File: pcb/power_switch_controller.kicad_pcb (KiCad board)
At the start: 2 copper layers, 116.8 x 53.3 mm, 19 parts, among them J1 DB15FV, J2 DB15FV, P1 PWR_JACK_2.5x5.5, P2 HEADER_01X03, U1 MAX6817

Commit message: Made design changes preparing for version 1.0.
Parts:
- removed J1, J2: DB15FV, aalborg_mfc_interface:DB15FD
- removed R3, R4: 5.11k, aalborg_mfc_interface:SM1210
- added D10, D6, D7, D8, D9: LED_24V, power_switch_controller:LED_555-3XXX, F.Cu at (152.4, 139.7)
- added D11: LED_24V, power_switch_controller:LED_555-3XXX, F.Cu at (130.8, 153.7)
- added D12: LED_24V, power_switch_controller:LED_555-3XXX, F.Cu at (123.2, 154.3)
- added D13: LED_24V, power_switch_controller:LED_555-3XXX, F.Cu at (114.9, 155.6)
- added D14: LED_24V, power_switch_controller:LED_555-3XXX, F.Cu at (104.8, 144.8)
- added D15: LED_24V, power_switch_controller:LED_555-3XXX, F.Cu at (165.7, 137.2)
- added D16: LED_24V, power_switch_controller:LED_555-3XXX, F.Cu at (122.6, 142.2)
- added D17: LED_24V, power_switch_controller:LED_555-3XXX, F.Cu at (139.1, 140.3)
- added D2: LED_24V, power_switch_controller:LED_555-3XXX, F.Cu at (181.0, 99.7)
- added D3: LED_24V, power_switch_controller:LED_555-3XXX, F.Cu at (172.1, 99.7)
- added D4: LED_24V, power_switch_controller:LED_555-3XXX, F.Cu at (163.2, 99.7)
- added D5: LED_24V, power_switch_controller:LED_555-3XXX, F.Cu at (154.3, 99.7)
- added RJ1: RJ45_DOUBLE, power_switch_controller:RJ45_2PORT_2ROW, F.Cu at (97.2, 94.0)
- added RJ2: RJ45_DOUBLE, power_switch_controller:RJ45_2PORT_2ROW, F.Cu at (97.2, 111.8)
- added S1: HEADER_01X02_POL, power_switch_controller:Header_Shrouded_2_Pin, F.Cu at (181.0, 95.9)
- added S10: HEADER_01X02_POL, power_switch_controller:Header_Shrouded_2_Pin, F.Cu at (153.0, 155.6)
- added S11: HEADER_01X02_POL, power_switch_controller:Header_Shrouded_2_Pin, F.Cu at (151.1, 163.8)
- added S12: HEADER_01X02_POL, power_switch_controller:Header_Shrouded_2_Pin, F.Cu at (144.1, 152.4)
- added S13: HEADER_01X02_POL, power_switch_controller:Header_Shrouded_2_Pin, F.Cu at (178.4, 142.2)
- added S14, S15, S16: HEADER_01X02_POL, power_switch_controller:Header_Shrouded_2_Pin, F.Cu at (179.7, 150.4)
- added S2: HEADER_01X02_POL, power_switch_controller:Header_Shrouded_2_Pin, F.Cu at (172.1, 95.9)
- added S3: HEADER_01X02_POL, power_switch_controller:Header_Shrouded_2_Pin, F.Cu at (163.2, 95.9)
- added S4: HEADER_01X02_POL, power_switch_controller:Header_Shrouded_2_Pin, F.Cu at (154.3, 95.9)
- added S5: HEADER_01X02_POL, power_switch_controller:Header_Shrouded_2_Pin, F.Cu at (145.4, 95.9)
- added S6: HEADER_01X02_POL, power_switch_controller:Header_Shrouded_2_Pin, F.Cu at (136.5, 95.9)
- added S7: HEADER_01X02_POL, power_switch_controller:Header_Shrouded_2_Pin, F.Cu at (177.2, 158.8)
- added S8: HEADER_01X02_POL, power_switch_controller:Header_Shrouded_2_Pin, F.Cu at (167.0, 151.8)
- added S9: HEADER_01X02_POL, power_switch_controller:Header_Shrouded_2_Pin, F.Cu at (164.5, 161.9)
- added SW1: SPST_SERIES_M, power_switch_controller:SPST_SERIES_M, F.Cu at (202.6, 83.2)
- added U2: TLE723X, power_switch_controller:TLE723X, B.Cu at (149.9, 87.0)
- added U3: TLE723X, power_switch_controller:TLE723X, B.Cu at (149.9, 109.2)
- ARDUINO1: footprint aalborg_mfc_interface:ARDUINO_MEGA_SHIELD -> power_switch_controller:ARDUINO_MEGA_SHIELD
- C1, C2, C3, C4, R1, R2: footprint aalborg_mfc_interface:SM1210 -> power_switch_controller:SM1210
- C5: value 10uF -> 0.1uF; footprint aalborg_mfc_interface:SM1210 -> power_switch_controller:SM1210; moved to F.Cu
- C6: value 10uF -> 0.1uF; footprint aalborg_mfc_interface:SM1210 -> power_switch_controller:SM1210
- D1: footprint aalborg_mfc_interface:LED_555-3XXX -> power_switch_controller:LED_555-3XXX
- E1: footprint aalborg_mfc_interface:Micro-MaTch_6_SMD -> power_switch_controller:Micro-MaTch_6_SMD
- P1: footprint aalborg_mfc_interface:DCJACK_2PIN_HIGHCURRENT -> power_switch_controller:DCJACK_2PIN_HIGHCURRENT
- P2: footprint aalborg_mfc_interface:Header_Shrouded_3_Pin -> power_switch_controller:Header_Shrouded_3_Pin
- REG1: footprint aalborg_mfc_interface:DC_DC_CONV_R78C -> power_switch_controller:DC_DC_CONV_R78C
- U1: footprint aalborg_mfc_interface:MAX6817 -> power_switch_controller:MAX6817
- moved C5 77.7 mm to (202.6, 140.3), turned to 270 degrees
- moved D1 2.29 mm to (202.6, 92.7)
- moved C3 2.01 mm to (104.8, 127.0), turned to 180 degrees
- moved P2 2.01 mm to (103.5, 123.2)
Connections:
- ARDUINO1 pad 22: /PURGE_A -> (no net)
- ARDUINO1 pad 23: /VALVE_OFF_A -> (no net)
- ARDUINO1 pad 24: /PURGE_B -> (no net)
- ARDUINO1 pad 25: /VALVE_OFF_B -> (no net)
- ARDUINO1 pad 48: (no net) -> /IN
- ARDUINO1 pad 49: (no net) -> /CS
- ARDUINO1 pad 50: (no net) -> /MISO
- ARDUINO1 pad 51: (no net) -> /MOSI
- ARDUINO1 pad 52: (no net) -> /SCK
- ARDUINO1 pad 7: /PWM_A -> (no net)
- ARDUINO1 pad 8: /PWM_B -> (no net)
- ARDUINO1 pad A0: /ANALOG_IN_A -> (no net)
- ARDUINO1 pad A1: /ANALOG_IN_B -> (no net)
- ARDUINO1 pad RST: (no net) -> /RST
- C5 pad 1: /ANALOG_OUT_A -> +5V
- C6 pad 1: /ANALOG_OUT_B -> +5V
- D1 pad 1: VAA -> /LED_PWR
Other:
- board text added: "Janelia Remote Device power_switch_controller model_number: 1101 01/2015 version 1.0"
- board text removed: "Janelia Remote Device aalborg_mfc_interface model_number: 1100 12/2014 version 1.1"
- board text removed: "MFCA"
- board text removed: "MFCB"

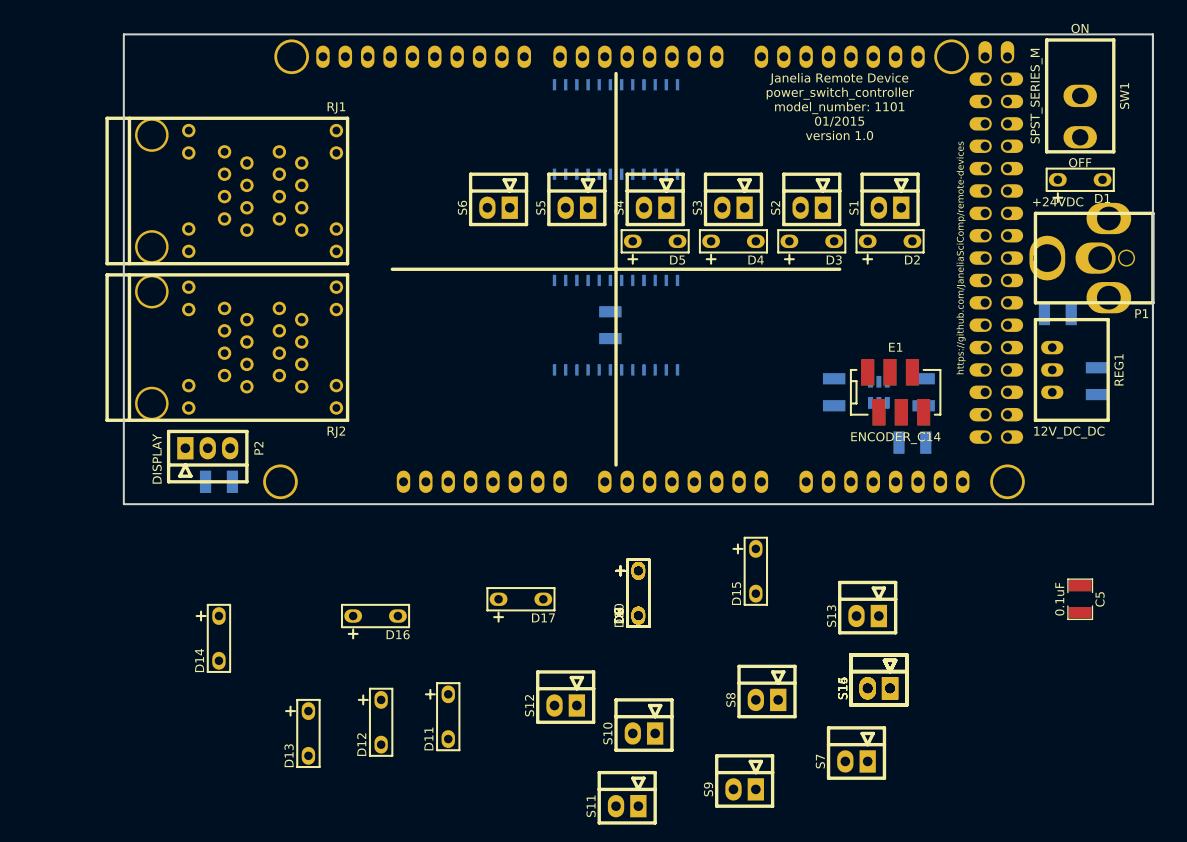
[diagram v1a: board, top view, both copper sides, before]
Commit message: Changed connectors to 2x16 header.
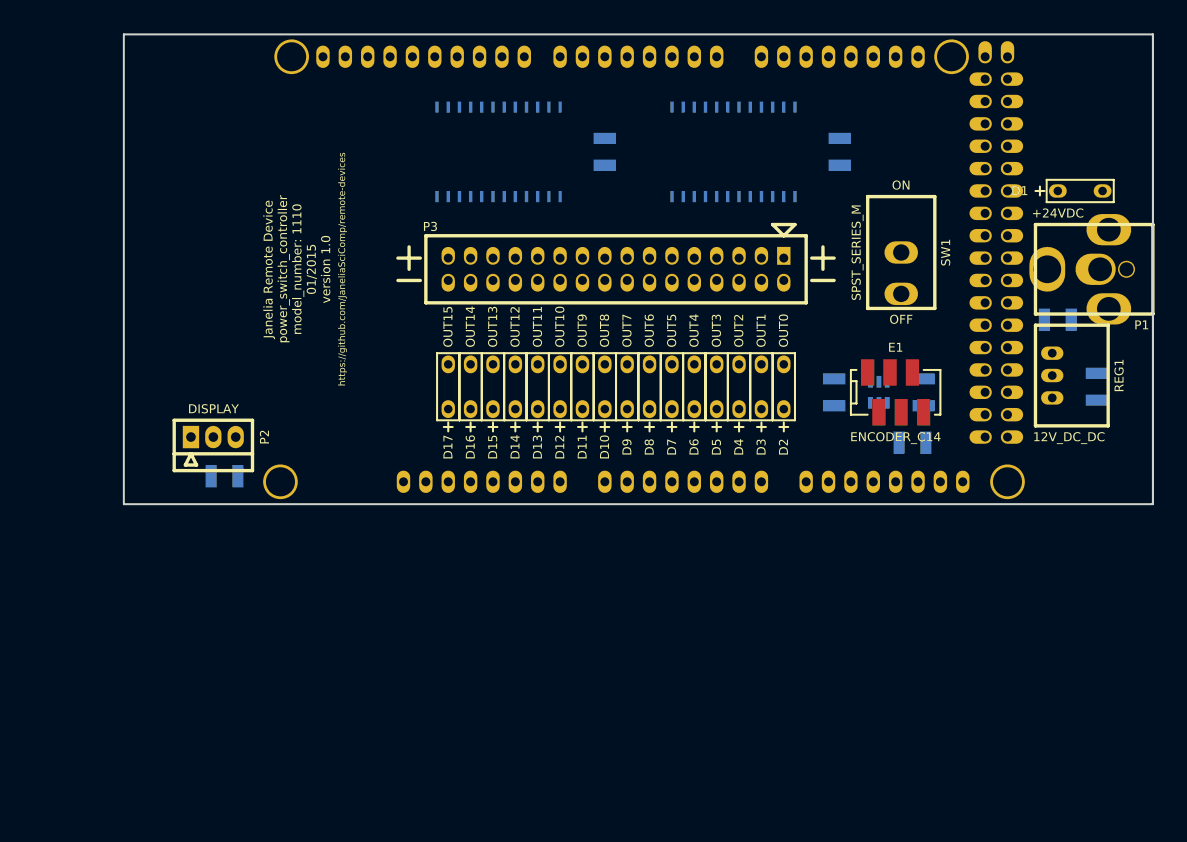
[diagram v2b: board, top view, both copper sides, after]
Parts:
- removed RJ1, RJ2: RJ45_DOUBLE, power_switch_controller:RJ45_2PORT_2ROW
- removed S1, S10, S11, S12, S13, S14, S15, S16, S2, S3, S4, S5, S6, S7, S8, S9: HEADER_01X02_POL, power_switch_controller:Header_Shrouded_2_Pin
- added P3: HEADER_02X16, power_switch_controller:HEADER_02x32, F.Cu at (149.9, 102.9)
- C5: moved to B.Cu
- moved C5 57.7 mm to (175.3, 89.5)
- moved D13 47.2 mm to (141.0, 116.2), turned to 180 degrees
- moved D14 44.1 mm to (138.4, 116.2), turned to 180 degrees
- moved D12 43.2 mm to (143.5, 116.2), turned to 180 degrees
- moved D11 40.4 mm to (146.1, 116.2), turned to 180 degrees
- moved D15 36.5 mm to (135.9, 116.2), turned to 180 degrees
- moved D16 28.2 mm to (133.3, 116.2), turned to 180 degrees
- moved SW1 27.0 mm to (182.2, 101.0)
- moved D17 25.5 mm to (130.8, 116.2), turned to 180 degrees
- moved D6 24.3 mm to (158.8, 116.2), turned to 180 degrees
- moved U3 23.8 mm to (136.5, 89.5)
- moved D10 23.8 mm to (148.6, 116.2), turned to 180 degrees
- moved D7 23.8 mm to (156.2, 116.2), turned to 180 degrees
- moved D8 23.5 mm to (153.7, 116.2), turned to 180 degrees
- moved D9 23.5 mm to (151.1, 116.2), turned to 180 degrees
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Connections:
- net /SO1 renamed /SI1
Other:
- board text added: "Janelia Remote Device power_switch_controller model_number: 1110 01/2015 version 1.0"
- board text added: "OUT0"
- board text added: "OUT1"
- board text added: "OUT10"
- board text added: "OUT11"
- board text added: "OUT12"
- board text added: "OUT13"
- board text added: "OUT14"
- board text added: "OUT15"
- board text added: "OUT2"
- board text added: "OUT3"
- board text added: "OUT4"
- board text added: "OUT5"
- board text added: "OUT6"
- board text added: "OUT7"
- board text added: "OUT8"
- board text added: "OUT9"
- board text removed: "Janelia Remote Device power_switch_controller model_number: 1101 01/2015 version 1.0"

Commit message: Moved components on pcb.
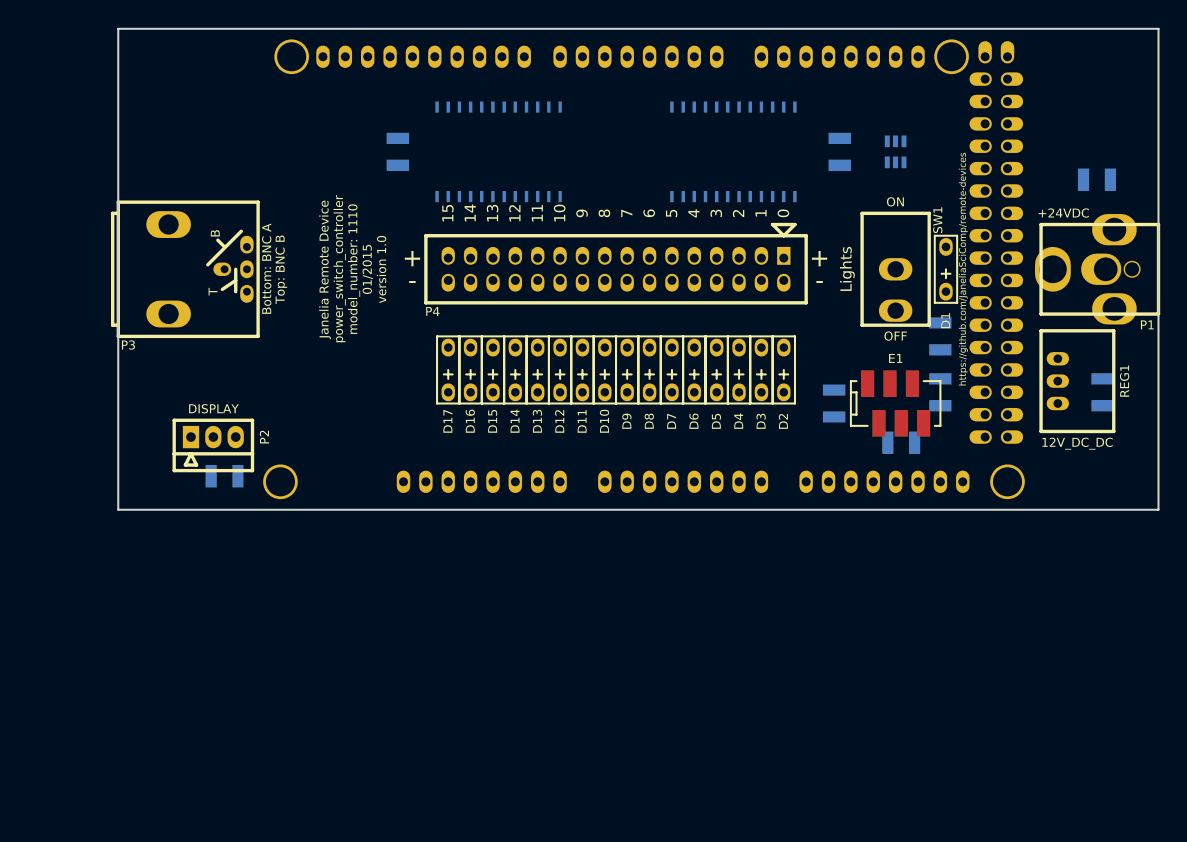
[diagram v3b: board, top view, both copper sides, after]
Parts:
- added P4: HEADER_02X16, power_switch_controller:HEADER_02x32, F.Cu at (149.9, 102.9)
- added R3: 5.11k, power_switch_controller:SM1210, B.Cu at (186.7, 110.5)
- P3: value HEADER_02X16 -> BNC_DOUBLE_RA; footprint power_switch_controller:HEADER_02x32 -> power_switch_controller:BNC_DOUBLE
- moved P3 50.8 mm to (99.1, 102.9), turned to 90 degrees
- moved U1 27.4 mm to (181.6, 89.5), turned to 90 degrees
- moved C6 23.5 mm to (125.1, 89.5), turned to 90 degrees
- moved D1 17.6 mm to (187.3, 102.9), turned to 180 degrees
- moved C1 16.5 mm to (204.5, 92.7)
- moved R2 9.94 mm to (174.6, 118.1), turned to 270 degrees
- moved C4 9.53 mm to (182.2, 122.6), turned to 180 degrees
- moved SW1 2.01 mm to (181.6, 102.9)
- moved D10 1.91 mm to (148.6, 114.3)
- moved D11 1.91 mm to (146.1, 114.3)
- moved D12 1.91 mm to (143.5, 114.3)
- moved D13 1.91 mm to (141.0, 114.3)
- moved D14 1.91 mm to (138.4, 114.3)
- moved D15 1.91 mm to (135.9, 114.3)
- moved D16 1.91 mm to (133.3, 114.3)
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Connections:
- ARDUINO1 pad 18: (no net) -> /D_LED_PWR
- ARDUINO1 pad 20: Net-(ARDUINO1-Pad20) -> (no net)
- ARDUINO1 pad 21: Net-(ARDUINO1-Pad21) -> (no net)
- P3 pad 1: VAA -> /BNC_A
- P3 pad 2: /OUT0 -> GND
- P3 pad 3: VAA -> /BNC_B
- P3 pad 4: /OUT1 -> GND
- U1 pad 3: (no net) -> /LED_PWR
- U1 pad 4: (no net) -> /D_LED_PWR
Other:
- board size 116.8 x 53.3 mm -> 118.1 x 54.6 mm
- net class SUPERPOWER added: clearance 0.254, trace_width 1.2192, via_dia 0.889, via_drill 0.635
- board text removed: "OUT0"
- board text removed: "OUT1"
- board text removed: "OUT10"
- board text removed: "OUT11"
- board text removed: "OUT12"
- board text removed: "OUT13"
- board text removed: "OUT14"
- board text removed: "OUT15"
- board text removed: "OUT2"
- board text removed: "OUT3"
- board text removed: "OUT4"
- board text removed: "OUT5"
- board text removed: "OUT6"
- board text removed: "OUT7"
- board text removed: "OUT8"
- board text removed: "OUT9"

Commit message: Finished pcb version 1.0
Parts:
- added P5: HEADER_02X08, power_switch_controller:HEADER_02x08, F.Cu at (129.5, 102.9)
- P4: value HEADER_02X16 -> HEADER_02X08; footprint power_switch_controller:HEADER_02x32 -> power_switch_controller:HEADER_02x08
- moved D11 10.2 mm to (135.9, 114.9)
- moved D10 10.2 mm to (138.4, 114.9)
- moved D12 10.2 mm to (133.3, 114.9)
- moved D13 10.2 mm to (130.8, 114.9)
- moved D14 10.2 mm to (128.3, 114.9)
- moved D16 10.2 mm to (123.2, 114.9)
- moved D17 10.2 mm to (120.7, 114.9)
- moved D15 10.2 mm to (125.7, 114.9)
- moved P4 10.2 mm to (160.0, 102.9)
- moved C6 7.62 mm to (117.5, 89.5)
- moved U3 6.99 mm to (129.5, 89.5)
- moved C5 3.17 mm to (172.1, 89.5)
- moved U2 3.17 mm to (160.0, 89.5)
- moved D2 0.64 mm to (168.9, 114.9)
- moved D3 0.64 mm to (166.4, 114.9)
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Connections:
- ARDUINO1 pad 10: (no net) -> /BNC_B
- ARDUINO1 pad 20B: /BNC_B -> (no net)
- ARDUINO1 pad 21B: /BNC_A -> (no net)
- ARDUINO1 pad A0: (no net) -> /BNC_A
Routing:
- net GND: track 0.00 -> 327.8 mm, vias 0 -> 3
- net +5V: track 0.00 -> 273.5 mm, vias 0 -> 2
- net VAA: track 0.00 -> 128.2 mm
- net /ENC_B: track 0.00 -> 111.3 mm, vias 0 -> 1
- net /SCK: track 0.00 -> 99.8 mm, vias 0 -> 3
- net /TX3: track 0.00 -> 97.1 mm
- net /LED_PWR: track 0.00 -> 92.6 mm
- net /MISO: track 0.00 -> 84.4 mm, vias 0 -> 1
- net /RST: track 0.00 -> 79.4 mm
- net /ENC_A: track 0.00 -> 75.7 mm, vias 0 -> 1
- net /CS: track 0.00 -> 74.4 mm, vias 0 -> 2
- net /OUT1: track 0.00 -> 71.6 mm
- net /IN: track 0.00 -> 71.1 mm, vias 0 -> 2
- net /V_IN: track 0.00 -> 70.1 mm
- net /MOSI: track 0.00 -> 67.9 mm, vias 0 -> 1
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- added copper zone on B.Cu, net GND
- added copper zone on F.Cu, net VAA
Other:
- net class SUPERPOWER: trace_width 1.2192 -> 1.016
- board text added: "+"
- board text added: "-"
- board text added: "0"
- board text added: "1"
- board text added: "10"
- board text added: "11"
- board text added: "12"
- board text added: "13"
- board text added: "14"
- board text added: "15"
- board text added: "2"
- board text added: "3"
- board text added: "4"
- board text added: "5"
- board text added: "6"
- board text added: "7"
- board text added: "8"
- board text added: "9"
